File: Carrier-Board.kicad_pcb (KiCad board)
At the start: 2 copper layers, 92 x 96 mm, 42 parts, among them J1 CONN_3-6318491-6, J10 Conn_02x03_Odd_Even, J2 Conn_01x0, J3 Conn_02x26_Odd_Even, J4 SI-51009-F, J5 Conn_02x26_Odd_Even, J6 Conn_01x03_Male, J7 Conn_01x03_Male, J8 Conn_01x06_Male, J9 Conn_02x04_Odd_Even, SW1 SW_Push, SW2 SW_Push, SW3 SW_Push, U1 MPM3620, U2 MPM3620, U9 MSATA-Socket

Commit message: Change but3ton footprint
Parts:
- SW1, SW2, SW3: footprint Buttons_Switches_SMD:SW_SPST_PTS645 -> Buttons_Switches_SMD:SW_SPST_B3U-1000P
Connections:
- J1 pad 101: Net-(J1-Pad101) -> (no net)
- J1 pad 102: Net-(J1-Pad102) -> (no net)
- J1 pad 103: Net-(J1-Pad103) -> (no net)
- J1 pad 112: Net-(J1-Pad112) -> (no net)
- J1 pad 113: Net-(J1-Pad113) -> (no net)
- J1 pad 114: Net-(J1-Pad114) -> (no net)
- J1 pad 115: Net-(J1-Pad115) -> (no net)
- J1 pad 123: Net-(J1-Pad123) -> (no net)
- J1 pad 124: Net-(J1-Pad124) -> (no net)
- J1 pad 125: Net-(J1-Pad125) -> (no net)
- J1 pad 126: Net-(J1-Pad126) -> (no net)
- J1 pad 127: Net-(J1-Pad127) -> (no net)
- J1 pad 128: Net-(J1-Pad128) -> (no net)
- J1 pad 129: Net-(J1-Pad129) -> (no net)
- J1 pad 130: Net-(J1-Pad130) -> (no net)
- J1 pad 132: Net-(J1-Pad132) -> (no net)
- J1 pad 133: Net-(J1-Pad133) -> (no net)
- J1 pad 135: Net-(J1-Pad135) -> (no net)
- J1 pad 136: Net-(J1-Pad136) -> (no net)
- J1 pad 137: Net-(J1-Pad137) -> (no net)
- J1 pad 138: Net-(J1-Pad138) -> (no net)
- J1 pad 139: Net-(J1-Pad139) -> (no net)
- J1 pad 140: Net-(J1-Pad140) -> (no net)
- J1 pad 142: Net-(J1-Pad142) -> (no net)
- J1 pad 145: Net-(J1-Pad145) -> (no net)
- J1 pad 146: Net-(J1-Pad146) -> (no net)
- J1 pad 147: Net-(J1-Pad147) -> (no net)
- J1 pad 148: Net-(J1-Pad148) -> (no net)
- J1 pad 149: Net-(J1-Pad149) -> (no net)
- J1 pad 15: Net-(J1-Pad15) -> (no net)
- J1 pad 150: Net-(J1-Pad150) -> (no net)
- J1 pad 152: Net-(J1-Pad152) -> (no net)
- J1 pad 153: Net-(J1-Pad153) -> (no net)
- J1 pad 154: Net-(J1-Pad154) -> (no net)
- J1 pad 155: Net-(J1-Pad155) -> (no net)
- J1 pad 156: Net-(J1-Pad156) -> (no net)
- J1 pad 157: Net-(J1-Pad157) -> (no net)
- J1 pad 158: Net-(J1-Pad158) -> (no net)
- J1 pad 160: Net-(J1-Pad160) -> (no net)
- J1 pad 162: Net-(J1-Pad162) -> (no net)
- J1 pad 163: Net-(J1-Pad163) -> (no net)
- J1 pad 165: Net-(J1-Pad165) -> (no net)
- J1 pad 166: Net-(J1-Pad166) -> (no net)
- J1 pad 168: Net-(J1-Pad168) -> (no net)
- J1 pad 169: Net-(J1-Pad169) -> (no net)
- J1 pad 171: Net-(J1-Pad171) -> (no net)
- J1 pad 172: Net-(J1-Pad172) -> (no net)
- J1 pad 174: Net-(J1-Pad174) -> (no net)
- J1 pad 175: Net-(J1-Pad175) -> (no net)
- J1 pad 176: Net-(J1-Pad176) -> (no net)
- J1 pad 178: Net-(J1-Pad178) -> (no net)
- J1 pad 179: Net-(J1-Pad179) -> (no net)
- J1 pad 18: Net-(J1-Pad18) -> (no net)
- J1 pad 181: Net-(J1-Pad181) -> (no net)
- J1 pad 182: Net-(J1-Pad182) -> (no net)
- J1 pad 183: Net-(J1-Pad183) -> (no net)
- J1 pad 184: Net-(J1-Pad184) -> (no net)
- J1 pad 185: Net-(J1-Pad185) -> (no net)
- J1 pad 186: Net-(J1-Pad186) -> (no net)
- J1 pad 187: Net-(J1-Pad187) -> (no net)
- J1 pad 188: Net-(J1-Pad188) -> (no net)
- J1 pad 189: Net-(J1-Pad189) -> (no net)
- J1 pad 191: Net-(J1-Pad191) -> (no net)
- J1 pad 192: Net-(J1-Pad192) -> (no net)
- J1 pad 193: Net-(J1-Pad193) -> (no net)
- J1 pad 198: Net-(J1-Pad198) -> (no net)
- J1 pad 199: Net-(J1-Pad199) -> (no net)
- J1 pad 201: Net-(J1-Pad201) -> (no net)
- J1 pad 202: Net-(J1-Pad202) -> (no net)
- J1 pad 203: Net-(J1-Pad203) -> (no net)
- J1 pad 204: Net-(J1-Pad204) -> (no net)
- J1 pad 205: Net-(J1-Pad205) -> (no net)
- J1 pad 206: Net-(J1-Pad206) -> (no net)
- J1 pad 207: Net-(J1-Pad207) -> (no net)
- J1 pad 208: Net-(J1-Pad208) -> (no net)
- J1 pad 209: Net-(J1-Pad209) -> (no net)
- J1 pad 211: Net-(J1-Pad211) -> (no net)
- J1 pad 212: Net-(J1-Pad212) -> (no net)
- J1 pad 22: Net-(J1-Pad22) -> (no net)
- J1 pad 23: Net-(J1-Pad23) -> (no net)
- J1 pad 24: Net-(J1-Pad24) -> (no net)
- J1 pad 25: Net-(J1-Pad25) -> (no net)
- J1 pad 26: Net-(J1-Pad26) -> (no net)
- J1 pad 27: Net-(J1-Pad27) -> (no net)
- J1 pad 29: Net-(J1-Pad29) -> (no net)
- J1 pad 30: Net-(J1-Pad30) -> (no net)
- J1 pad 32: Net-(J1-Pad32) -> (no net)
- J1 pad 33: Net-(J1-Pad33) -> (no net)
- J1 pad 34: Net-(J1-Pad34) -> (no net)
- J1 pad 35: Net-(J1-Pad35) -> (no net)
- J1 pad 36: Net-(J1-Pad36) -> (no net)
- J1 pad 37: Net-(J1-Pad37) -> (no net)
- J1 pad 38: Net-(J1-Pad38) -> (no net)
- J1 pad 39: Net-(J1-Pad39) -> (no net)
- J1 pad 40: Net-(J1-Pad40) -> (no net)
- J1 pad 42: Net-(J1-Pad42) -> (no net)
- J1 pad 43: Net-(J1-Pad43) -> (no net)
- J1 pad 44: Net-(J1-Pad44) -> (no net)
- J1 pad 45: Net-(J1-Pad45) -> (no net)
- J1 pad 46: Net-(J1-Pad46) -> (no net)
- J1 pad 47: Net-(J1-Pad47) -> (no net)
- J1 pad 48: Net-(J1-Pad48) -> (no net)
- J1 pad 49: Net-(J1-Pad49) -> (no net)
- J1 pad 50: Net-(J1-Pad50) -> (no net)
- J1 pad 52: Net-(J1-Pad52) -> (no net)
- J1 pad 53: Net-(J1-Pad53) -> (no net)
- J1 pad 55: Net-(J1-Pad55) -> (no net)
- J1 pad 56: Net-(J1-Pad56) -> (no net)
- J1 pad 58: Net-(J1-Pad58) -> (no net)
- J1 pad 59: Net-(J1-Pad59) -> (no net)
- J1 pad 61: Net-(J1-Pad61) -> (no net)
- J1 pad 62: Net-(J1-Pad62) -> (no net)
- J1 pad 64: Net-(J1-Pad64) -> (no net)
- J1 pad 65: Net-(J1-Pad65) -> (no net)
- J1 pad 68: Net-(J1-Pad68) -> (no net)
- J1 pad 69: Net-(J1-Pad69) -> (no net)
- J1 pad 71: Net-(J1-Pad71) -> (no net)
- J1 pad 72: Net-(J1-Pad72) -> (no net)
- J1 pad 73: Net-(J1-Pad73) -> (no net)
- J1 pad 74: Net-(J1-Pad74) -> (no net)
- J1 pad 75: Net-(J1-Pad75) -> (no net)
- J1 pad 76: Net-(J1-Pad76) -> (no net)
- J1 pad 77: Net-(J1-Pad77) -> (no net)
- J1 pad 78: Net-(J1-Pad78) -> (no net)
- J1 pad 79: Net-(J1-Pad79) -> (no net)
- J1 pad 8: Net-(J1-Pad8) -> (no net)
- J1 pad 81: Net-(J1-Pad81) -> (no net)
- J1 pad 82: Net-(J1-Pad82) -> (no net)
- J1 pad 83: Net-(J1-Pad83) -> (no net)
- J1 pad 84: Net-(J1-Pad84) -> (no net)
- J1 pad 86: Net-(J1-Pad86) -> (no net)
- J1 pad 87: Net-(J1-Pad87) -> (no net)
- J1 pad 88: Net-(J1-Pad88) -> (no net)
- J1 pad 89: Net-(J1-Pad89) -> (no net)
- J1 pad 91: Net-(J1-Pad91) -> (no net)
- J1 pad 96: Net-(J1-Pad96) -> (no net)
- J10 pad 2: SPI_POWER -> (no net)
- J3 pad 1: Net-(J3-Pad1) -> (no net)
- J3 pad 10: Net-(J3-Pad10) -> (no net)
- J3 pad 11: Net-(J3-Pad11) -> (no net)
- J3 pad 12: Net-(J3-Pad12) -> (no net)
- J3 pad 13: Net-(J3-Pad13) -> (no net)
- J3 pad 14: Net-(J3-Pad14) -> (no net)
- J3 pad 15: Net-(J3-Pad15) -> (no net)
- J3 pad 16: Net-(J3-Pad16) -> (no net)
- J3 pad 17: Net-(J3-Pad17) -> (no net)
- J3 pad 18: Net-(J3-Pad18) -> (no net)
- J3 pad 19: Net-(J3-Pad19) -> (no net)
- J3 pad 2: Net-(J3-Pad2) -> (no net)
- J3 pad 20: Net-(J3-Pad20) -> (no net)
- J3 pad 21: Net-(J3-Pad21) -> (no net)
- J3 pad 22: Net-(J3-Pad22) -> (no net)
- J3 pad 23: Net-(J3-Pad23) -> (no net)
- J3 pad 24: Net-(J3-Pad24) -> (no net)
- J3 pad 25: Net-(J3-Pad25) -> (no net)
- J3 pad 26: Net-(J3-Pad26) -> (no net)
- J3 pad 27: Net-(J3-Pad27) -> (no net)
- J3 pad 28: Net-(J3-Pad28) -> (no net)
- J3 pad 29: Net-(J3-Pad29) -> (no net)
- J3 pad 3: Net-(J3-Pad3) -> (no net)
- J3 pad 30: Net-(J3-Pad30) -> (no net)
- J3 pad 31: Net-(J3-Pad31) -> (no net)
- J3 pad 32: Net-(J3-Pad32) -> (no net)
- J3 pad 33: Net-(J3-Pad33) -> (no net)
- J3 pad 34: Net-(J3-Pad34) -> (no net)
- J3 pad 35: Net-(J3-Pad35) -> (no net)
- J3 pad 36: Net-(J3-Pad36) -> (no net)
- J3 pad 37: Net-(J3-Pad37) -> (no net)
- J3 pad 38: Net-(J3-Pad38) -> (no net)
- J3 pad 39: Net-(J3-Pad39) -> (no net)
- J3 pad 4: Net-(J3-Pad4) -> (no net)
- J3 pad 40: Net-(J3-Pad40) -> (no net)
- J3 pad 41: Net-(J3-Pad41) -> (no net)
- J3 pad 42: Net-(J3-Pad42) -> (no net)
- J3 pad 43: Net-(J3-Pad43) -> (no net)
- J3 pad 44: Net-(J3-Pad44) -> (no net)
- J3 pad 45: Net-(J3-Pad45) -> (no net)
- J3 pad 46: Net-(J3-Pad46) -> (no net)
- J3 pad 47: Net-(J3-Pad47) -> (no net)
- J3 pad 48: Net-(J3-Pad48) -> (no net)
- J3 pad 49: Net-(J3-Pad49) -> (no net)
- J3 pad 5: Net-(J3-Pad5) -> (no net)
- J3 pad 50: Net-(J3-Pad50) -> (no net)
- J3 pad 51: Net-(J3-Pad51) -> (no net)
- J3 pad 52: Net-(J3-Pad52) -> (no net)
- J3 pad 6: Net-(J3-Pad6) -> (no net)
- J3 pad 7: Net-(J3-Pad7) -> (no net)
- J3 pad 8: Net-(J3-Pad8) -> (no net)
- J3 pad 9: Net-(J3-Pad9) -> (no net)
- J4 pad 14: Net-(J4-Pad14) -> (no net)
- J5 pad 1: Net-(J5-Pad1) -> (no net)
- J5 pad 10: Net-(J5-Pad10) -> (no net)
- J5 pad 11: Net-(J5-Pad11) -> (no net)
- J5 pad 12: Net-(J5-Pad12) -> (no net)
- J5 pad 13: Net-(J5-Pad13) -> (no net)
- J5 pad 14: Net-(J5-Pad14) -> (no net)
- J5 pad 15: Net-(J5-Pad15) -> (no net)
- J5 pad 16: Net-(J5-Pad16) -> (no net)
- J5 pad 17: Net-(J5-Pad17) -> (no net)
- J5 pad 18: Net-(J5-Pad18) -> (no net)
- J5 pad 19: Net-(J5-Pad19) -> (no net)
- J5 pad 2: Net-(J5-Pad2) -> (no net)
- J5 pad 20: Net-(J5-Pad20) -> (no net)
- J5 pad 21: Net-(J5-Pad21) -> (no net)
- J5 pad 22: Net-(J5-Pad22) -> (no net)
- J5 pad 23: Net-(J5-Pad23) -> (no net)
- J5 pad 24: Net-(J5-Pad24) -> (no net)
- J5 pad 25: Net-(J5-Pad25) -> (no net)
- J5 pad 26: Net-(J5-Pad26) -> (no net)
- J5 pad 27: Net-(J5-Pad27) -> (no net)
- J5 pad 28: Net-(J5-Pad28) -> (no net)
- J5 pad 29: Net-(J5-Pad29) -> (no net)
- J5 pad 3: Net-(J5-Pad3) -> (no net)
- J5 pad 30: Net-(J5-Pad30) -> (no net)
- J5 pad 31: Net-(J5-Pad31) -> (no net)
- J5 pad 32: Net-(J5-Pad32) -> (no net)
- J5 pad 33: Net-(J5-Pad33) -> (no net)
- J5 pad 34: Net-(J5-Pad34) -> (no net)
- J5 pad 35: Net-(J5-Pad35) -> (no net)
- J5 pad 36: Net-(J5-Pad36) -> (no net)
- J5 pad 37: Net-(J5-Pad37) -> (no net)
- J5 pad 38: Net-(J5-Pad38) -> (no net)
- J5 pad 39: Net-(J5-Pad39) -> (no net)
- J5 pad 4: Net-(J5-Pad4) -> (no net)
- J5 pad 40: Net-(J5-Pad40) -> (no net)
- J5 pad 41: Net-(J5-Pad41) -> (no net)
- J5 pad 42: Net-(J5-Pad42) -> (no net)
- J5 pad 43: Net-(J5-Pad43) -> (no net)
- J5 pad 44: Net-(J5-Pad44) -> (no net)
- J5 pad 45: Net-(J5-Pad45) -> (no net)
- J5 pad 46: Net-(J5-Pad46) -> (no net)
- J5 pad 47: Net-(J5-Pad47) -> (no net)
- J5 pad 48: Net-(J5-Pad48) -> (no net)
- J5 pad 49: Net-(J5-Pad49) -> (no net)
- J5 pad 5: Net-(J5-Pad5) -> (no net)
- J5 pad 50: Net-(J5-Pad50) -> (no net)
- J5 pad 51: Net-(J5-Pad51) -> (no net)
- J5 pad 52: Net-(J5-Pad52) -> (no net)
- J5 pad 6: Net-(J5-Pad6) -> (no net)
- J5 pad 7: Net-(J5-Pad7) -> (no net)
- J5 pad 8: Net-(J5-Pad8) -> (no net)
- J5 pad 9: Net-(J5-Pad9) -> (no net)
- J6 pad 1: Net-(J6-Pad1) -> (no net)
- U1 pad 11: Net-(U1-Pad11) -> (no net)
- U1 pad 2: Net-(U1-Pad2) -> (no net)
- U1 pad 4: Net-(U1-Pad4) -> (no net)
- U1 pad 5: Net-(U1-Pad5) -> (no net)
- U1 pad 6: Net-(U1-Pad6) -> (no net)
- U2 pad 11: Net-(U2-Pad11) -> (no net)
- U2 pad 2: Net-(U2-Pad2) -> (no net)
- U2 pad 4: Net-(U2-Pad4) -> (no net)
- U2 pad 5: Net-(U2-Pad5) -> (no net)
- U2 pad 6: Net-(U2-Pad6) -> (no net)
- U9 pad 1: Net-(U9-Pad1) -> (no net)
- U9 pad 10: Net-(U9-Pad10) -> (no net)
- U9 pad 11: Net-(U9-Pad11) -> (no net)
- U9 pad 12: Net-(U9-Pad12) -> (no net)
- U9 pad 13: Net-(U9-Pad13) -> (no net)
- U9 pad 14: Net-(U9-Pad14) -> (no net)
- U9 pad 16: Net-(U9-Pad16) -> (no net)
- U9 pad 17: Net-(U9-Pad17) -> (no net)
- U9 pad 19: Net-(U9-Pad19) -> (no net)
- U9 pad 20: Net-(U9-Pad20) -> (no net)
- U9 pad 22: Net-(U9-Pad22) -> (no net)
- U9 pad 28: Net-(U9-Pad28) -> (no net)
- U9 pad 3: Net-(U9-Pad3) -> (no net)
- U9 pad 30: Net-(U9-Pad30) -> (no net)
- U9 pad 32: Net-(U9-Pad32) -> (no net)
- U9 pad 36: Net-(U9-Pad36) -> (no net)
- U9 pad 38: Net-(U9-Pad38) -> (no net)
- U9 pad 42: Net-(U9-Pad42) -> (no net)
- U9 pad 43: Net-(U9-Pad43) -> (no net)
- U9 pad 44: Net-(U9-Pad44) -> (no net)
- U9 pad 45: Net-(U9-Pad45) -> (no net)
- U9 pad 46: Net-(U9-Pad46) -> (no net)
- U9 pad 47: Net-(U9-Pad47) -> (no net)
- U9 pad 48: Net-(U9-Pad48) -> (no net)
- U9 pad 5: Net-(U9-Pad5) -> (no net)
- U9 pad 6: Net-(U9-Pad6) -> (no net)
- U9 pad 7: Net-(U9-Pad7) -> (no net)
- U9 pad 8: Net-(U9-Pad8) -> (no net)

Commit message: started traces
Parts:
- added R10: 330, Resistors_SMD:R_0805, F.Cu at (155.5, 97.8)
- added R11: 10K, Resistors_SMD:R_0603, B.Cu at (87.6, 26.6)
- added R12: 10K, Resistors_SMD:R_0603, B.Cu at (89.4, 32.8)
- added R13: 10K, Resistors_SMD:R_0603, B.Cu at (89.4, 36.5)
- C1, C2, C3, C4: footprint BusSimulator:C22 -> Capacitors_SMD:C_0805; moved to F.Cu
- R1, R2, R3, R4, R5, R6, R7, R8, U1, U2: moved to F.Cu
- R32, R9: moved to B.Cu
- moved J6 89.4 mm to (169.7, 49.2), turned to 0 degrees
- moved J9 85.2 mm to (30.7, 35.5), turned to 0 degrees
- moved J10 83.3 mm to (61.4, 28.4), turned to 0 degrees
- moved R9 52.0 mm to (153.3, 96.1), turned to 270 degrees
- moved SW3 36.5 mm to (86.9, 36.4)
- moved SW2 29.9 mm to (86.9, 31.6)
- moved R25 28.7 mm to (130.0, 114.6), turned to 270 degrees
- moved D8 28.0 mm to (129.9, 113.9)
- moved R2 27.6 mm to (139.2, 108.8), turned to 180 degrees
- moved R1 25.9 mm to (142.4, 107.8), turned to 270 degrees
- moved C2 25.5 mm to (142.4, 104.0), turned to 90 degrees
- moved U1 25.3 mm to (137.9, 104.5)
- moved R4 22.6 mm to (133.9, 103.0), turned to 270 degrees
- moved D5 21.8 mm to (121.9, 111.2), turned to 270 degrees
- moved R3 21.7 mm to (136.9, 99.3), turned to 180 degrees
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- renumbered D7 to D6, D6 to D7
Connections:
- J1 pad 101: (no net) -> Net-(J1-Pad101)
- J1 pad 102: (no net) -> Net-(J1-Pad102)
- J1 pad 103: (no net) -> Net-(J1-Pad103)
- J1 pad 112: (no net) -> Net-(J1-Pad112)
- J1 pad 113: (no net) -> Net-(J1-Pad113)
- J1 pad 114: (no net) -> Net-(J1-Pad114)
- J1 pad 115: (no net) -> Net-(J1-Pad115)
- J1 pad 123: (no net) -> Net-(J1-Pad123)
- J1 pad 124: (no net) -> Net-(J1-Pad124)
- J1 pad 125: (no net) -> Net-(J1-Pad125)
- J1 pad 126: (no net) -> Net-(J1-Pad126)
- J1 pad 127: (no net) -> Net-(J1-Pad127)
- J1 pad 128: (no net) -> Net-(J1-Pad128)
- J1 pad 129: (no net) -> Net-(J1-Pad129)
- J1 pad 130: (no net) -> Net-(J1-Pad130)
- J1 pad 132: (no net) -> Net-(J1-Pad132)
- J1 pad 133: (no net) -> Net-(J1-Pad133)
- J1 pad 135: (no net) -> Net-(J1-Pad135)
- J1 pad 136: (no net) -> Net-(J1-Pad136)
- J1 pad 137: (no net) -> Net-(J1-Pad137)
- J1 pad 138: (no net) -> Net-(J1-Pad138)
- J1 pad 139: (no net) -> Net-(J1-Pad139)
- J1 pad 140: (no net) -> Net-(J1-Pad140)
- J1 pad 142: (no net) -> Net-(J1-Pad142)
- J1 pad 145: (no net) -> Net-(J1-Pad145)
- J1 pad 146: (no net) -> Net-(J1-Pad146)
- J1 pad 147: (no net) -> Net-(J1-Pad147)
- J1 pad 148: (no net) -> Net-(J1-Pad148)
- J1 pad 149: (no net) -> Net-(J1-Pad149)
- J1 pad 15: (no net) -> Net-(J1-Pad15)
- J1 pad 150: (no net) -> Net-(J1-Pad150)
- J1 pad 152: (no net) -> Net-(J1-Pad152)
- J1 pad 153: (no net) -> Net-(J1-Pad153)
- J1 pad 154: (no net) -> Net-(J1-Pad154)
- J1 pad 155: (no net) -> Net-(J1-Pad155)
- J1 pad 156: (no net) -> Net-(J1-Pad156)
- J1 pad 157: (no net) -> Net-(J1-Pad157)
- J1 pad 158: (no net) -> Net-(J1-Pad158)
- J1 pad 160: (no net) -> Net-(J1-Pad160)
- J1 pad 162: (no net) -> Net-(J1-Pad162)
- J1 pad 163: (no net) -> Net-(J1-Pad163)
- J1 pad 165: (no net) -> Net-(J1-Pad165)
- J1 pad 166: (no net) -> Net-(J1-Pad166)
- J1 pad 168: (no net) -> Net-(J1-Pad168)
- J1 pad 169: (no net) -> Net-(J1-Pad169)
- J1 pad 171: (no net) -> Net-(J1-Pad171)
- J1 pad 172: (no net) -> Net-(J1-Pad172)
- J1 pad 174: (no net) -> Net-(J1-Pad174)
- J1 pad 175: (no net) -> Net-(J1-Pad175)
- J1 pad 176: (no net) -> Net-(J1-Pad176)
- J1 pad 178: (no net) -> Net-(J1-Pad178)
- J1 pad 179: (no net) -> Net-(J1-Pad179)
- J1 pad 18: (no net) -> Net-(J1-Pad18)
- J1 pad 181: (no net) -> Net-(J1-Pad181)
- J1 pad 182: (no net) -> Net-(J1-Pad182)
- J1 pad 183: (no net) -> Net-(J1-Pad183)
- J1 pad 184: (no net) -> Net-(J1-Pad184)
- J1 pad 185: (no net) -> Net-(J1-Pad185)
- J1 pad 186: (no net) -> Net-(J1-Pad186)
- J1 pad 187: (no net) -> Net-(J1-Pad187)
- J1 pad 188: (no net) -> Net-(J1-Pad188)
- J1 pad 189: (no net) -> Net-(J1-Pad189)
- J1 pad 191: (no net) -> Net-(J1-Pad191)
- J1 pad 192: (no net) -> Net-(J1-Pad192)
- J1 pad 193: (no net) -> Net-(J1-Pad193)
- J1 pad 198: (no net) -> Net-(J1-Pad198)
- J1 pad 199: (no net) -> Net-(J1-Pad199)
- J1 pad 201: (no net) -> Net-(J1-Pad201)
- J1 pad 202: (no net) -> Net-(J1-Pad202)
- J1 pad 203: (no net) -> Net-(J1-Pad203)
- J1 pad 204: (no net) -> Net-(J1-Pad204)
- J1 pad 205: (no net) -> Net-(J1-Pad205)
- J1 pad 206: (no net) -> Net-(J1-Pad206)
- J1 pad 207: (no net) -> Net-(J1-Pad207)
- J1 pad 208: (no net) -> Net-(J1-Pad208)
- J1 pad 209: (no net) -> Net-(J1-Pad209)
- J1 pad 211: (no net) -> Net-(J1-Pad211)
- J1 pad 212: (no net) -> Net-(J1-Pad212)
- J1 pad 22: (no net) -> Net-(J1-Pad22)
- J1 pad 23: (no net) -> Net-(J1-Pad23)
- J1 pad 24: (no net) -> Net-(J1-Pad24)
- J1 pad 25: (no net) -> Net-(J1-Pad25)
- J1 pad 26: (no net) -> Net-(J1-Pad26)
- J1 pad 27: (no net) -> Net-(J1-Pad27)
- J1 pad 29: (no net) -> Net-(J1-Pad29)
- J1 pad 30: (no net) -> Net-(J1-Pad30)
- J1 pad 32: (no net) -> Net-(J1-Pad32)
- J1 pad 33: (no net) -> Net-(J1-Pad33)
- J1 pad 34: (no net) -> Net-(J1-Pad34)
- J1 pad 35: (no net) -> Net-(J1-Pad35)
- J1 pad 36: (no net) -> Net-(J1-Pad36)
- J1 pad 37: (no net) -> Net-(J1-Pad37)
- J1 pad 38: (no net) -> Net-(J1-Pad38)
- J1 pad 39: (no net) -> Net-(J1-Pad39)
- J1 pad 40: (no net) -> Net-(J1-Pad40)
- J1 pad 42: (no net) -> Net-(J1-Pad42)
- J1 pad 43: (no net) -> Net-(J1-Pad43)
- J1 pad 44: (no net) -> Net-(J1-Pad44)
- J1 pad 45: (no net) -> Net-(J1-Pad45)
- J1 pad 46: (no net) -> Net-(J1-Pad46)
- J1 pad 47: (no net) -> Net-(J1-Pad47)
- J1 pad 48: (no net) -> Net-(J1-Pad48)
- J1 pad 49: (no net) -> Net-(J1-Pad49)
- J1 pad 50: (no net) -> Net-(J1-Pad50)
- J1 pad 52: (no net) -> Net-(J1-Pad52)
- J1 pad 53: (no net) -> Net-(J1-Pad53)
- J1 pad 55: (no net) -> Net-(J1-Pad55)
- J1 pad 56: (no net) -> Net-(J1-Pad56)
- J1 pad 58: (no net) -> Net-(J1-Pad58)
- J1 pad 59: (no net) -> Net-(J1-Pad59)
- J1 pad 61: (no net) -> Net-(J1-Pad61)
- J1 pad 62: (no net) -> Net-(J1-Pad62)
- J1 pad 64: (no net) -> Net-(J1-Pad64)
- J1 pad 65: (no net) -> Net-(J1-Pad65)
- J1 pad 68: (no net) -> Net-(J1-Pad68)
- J1 pad 69: (no net) -> Net-(J1-Pad69)
- J1 pad 71: (no net) -> Net-(J1-Pad71)
- J1 pad 72: (no net) -> Net-(J1-Pad72)
- J1 pad 73: (no net) -> Net-(J1-Pad73)
- J1 pad 74: (no net) -> Net-(J1-Pad74)
- J1 pad 75: (no net) -> Net-(J1-Pad75)
- J1 pad 76: (no net) -> Net-(J1-Pad76)
- J1 pad 77: (no net) -> Net-(J1-Pad77)
- J1 pad 78: (no net) -> Net-(J1-Pad78)
- J1 pad 79: (no net) -> Net-(J1-Pad79)
- J1 pad 8: (no net) -> Net-(J1-Pad8)
- J1 pad 81: (no net) -> Net-(J1-Pad81)
- J1 pad 82: (no net) -> Net-(J1-Pad82)
- J1 pad 83: (no net) -> Net-(J1-Pad83)
- J1 pad 84: (no net) -> Net-(J1-Pad84)
- J1 pad 86: (no net) -> Net-(J1-Pad86)
- J1 pad 87: (no net) -> Net-(J1-Pad87)
- J1 pad 88: (no net) -> Net-(J1-Pad88)
- J1 pad 89: (no net) -> Net-(J1-Pad89)
- J1 pad 91: (no net) -> Net-(J1-Pad91)
- J1 pad 96: (no net) -> Net-(J1-Pad96)
- J1 pad TAB1: (no net) -> GBE0_CTREF(GND)
- J10 pad 2: (no net) -> SPI_POWER
- J3 pad 1: (no net) -> Net-(J3-Pad1)
- J3 pad 10: (no net) -> Net-(J3-Pad10)
- J3 pad 11: (no net) -> Net-(J3-Pad11)
- J3 pad 12: (no net) -> Net-(J3-Pad12)
- J3 pad 13: (no net) -> Net-(J3-Pad13)
- J3 pad 14: (no net) -> Net-(J3-Pad14)
- J3 pad 15: (no net) -> Net-(J3-Pad15)
- J3 pad 16: (no net) -> Net-(J3-Pad16)
- J3 pad 17: (no net) -> Net-(J3-Pad17)
- J3 pad 18: (no net) -> Net-(J3-Pad18)
- J3 pad 19: (no net) -> Net-(J3-Pad19)
- J3 pad 2: (no net) -> Net-(J3-Pad2)
- J3 pad 20: (no net) -> Net-(J3-Pad20)
- J3 pad 21: (no net) -> Net-(J3-Pad21)
- J3 pad 22: (no net) -> Net-(J3-Pad22)
- J3 pad 23: (no net) -> Net-(J3-Pad23)
- J3 pad 24: (no net) -> Net-(J3-Pad24)
- J3 pad 25: (no net) -> Net-(J3-Pad25)
- J3 pad 26: (no net) -> Net-(J3-Pad26)
- J3 pad 27: (no net) -> Net-(J3-Pad27)
- J3 pad 28: (no net) -> Net-(J3-Pad28)
- J3 pad 29: (no net) -> Net-(J3-Pad29)
- J3 pad 3: (no net) -> Net-(J3-Pad3)
- J3 pad 30: (no net) -> Net-(J3-Pad30)
- J3 pad 31: (no net) -> Net-(J3-Pad31)
- J3 pad 32: (no net) -> Net-(J3-Pad32)
- J3 pad 33: (no net) -> Net-(J3-Pad33)
- J3 pad 34: (no net) -> Net-(J3-Pad34)
- J3 pad 35: (no net) -> Net-(J3-Pad35)
- J3 pad 36: (no net) -> Net-(J3-Pad36)
- J3 pad 37: (no net) -> Net-(J3-Pad37)
- J3 pad 38: (no net) -> Net-(J3-Pad38)
- J3 pad 39: (no net) -> Net-(J3-Pad39)
- J3 pad 4: (no net) -> Net-(J3-Pad4)
- J3 pad 40: (no net) -> Net-(J3-Pad40)
- J3 pad 41: (no net) -> Net-(J3-Pad41)
- J3 pad 42: (no net) -> Net-(J3-Pad42)
- J3 pad 43: (no net) -> Net-(J3-Pad43)
- J3 pad 44: (no net) -> Net-(J3-Pad44)
- J3 pad 45: (no net) -> Net-(J3-Pad45)
- J3 pad 46: (no net) -> Net-(J3-Pad46)
- J3 pad 47: (no net) -> Net-(J3-Pad47)
- J3 pad 48: (no net) -> Net-(J3-Pad48)
- J3 pad 49: (no net) -> Net-(J3-Pad49)
- J3 pad 5: (no net) -> Net-(J3-Pad5)
- J3 pad 50: (no net) -> Net-(J3-Pad50)
- J3 pad 51: (no net) -> Net-(J3-Pad51)
- J3 pad 52: (no net) -> Net-(J3-Pad52)
- J3 pad 6: (no net) -> Net-(J3-Pad6)
- J3 pad 7: (no net) -> Net-(J3-Pad7)
- J3 pad 8: (no net) -> Net-(J3-Pad8)
- J3 pad 9: (no net) -> Net-(J3-Pad9)
- J4 pad 14: (no net) -> Net-(J4-Pad14)
- J5 pad 1: (no net) -> Net-(J5-Pad1)
- J5 pad 10: (no net) -> Net-(J5-Pad10)
- J5 pad 11: (no net) -> Net-(J5-Pad11)
- J5 pad 12: (no net) -> Net-(J5-Pad12)
- J5 pad 13: (no net) -> Net-(J5-Pad13)
- J5 pad 14: (no net) -> Net-(J5-Pad14)
- J5 pad 15: (no net) -> Net-(J5-Pad15)
- J5 pad 16: (no net) -> Net-(J5-Pad16)
- J5 pad 17: (no net) -> Net-(J5-Pad17)
- J5 pad 18: (no net) -> Net-(J5-Pad18)
- J5 pad 19: (no net) -> Net-(J5-Pad19)
- J5 pad 2: (no net) -> Net-(J5-Pad2)
- J5 pad 20: (no net) -> Net-(J5-Pad20)
- J5 pad 21: (no net) -> Net-(J5-Pad21)
- J5 pad 22: (no net) -> Net-(J5-Pad22)
- J5 pad 23: (no net) -> Net-(J5-Pad23)
- J5 pad 24: (no net) -> Net-(J5-Pad24)
- J5 pad 25: (no net) -> Net-(J5-Pad25)
- J5 pad 26: (no net) -> Net-(J5-Pad26)
- J5 pad 27: (no net) -> Net-(J5-Pad27)
- J5 pad 28: (no net) -> Net-(J5-Pad28)
- J5 pad 29: (no net) -> Net-(J5-Pad29)
- J5 pad 3: (no net) -> Net-(J5-Pad3)
- J5 pad 30: (no net) -> Net-(J5-Pad30)
- J5 pad 31: (no net) -> Net-(J5-Pad31)
- J5 pad 32: (no net) -> Net-(J5-Pad32)
- J5 pad 33: (no net) -> Net-(J5-Pad33)
- J5 pad 34: (no net) -> Net-(J5-Pad34)
- J5 pad 35: (no net) -> Net-(J5-Pad35)
- J5 pad 36: (no net) -> Net-(J5-Pad36)
- J5 pad 37: (no net) -> Net-(J5-Pad37)
- J5 pad 38: (no net) -> Net-(J5-Pad38)
- J5 pad 39: (no net) -> Net-(J5-Pad39)
- J5 pad 4: (no net) -> Net-(J5-Pad4)
- J5 pad 40: (no net) -> Net-(J5-Pad40)
- J5 pad 41: (no net) -> Net-(J5-Pad41)
- J5 pad 42: (no net) -> Net-(J5-Pad42)
- J5 pad 43: (no net) -> Net-(J5-Pad43)
- J5 pad 44: (no net) -> Net-(J5-Pad44)
- J5 pad 45: (no net) -> Net-(J5-Pad45)
- J5 pad 46: (no net) -> Net-(J5-Pad46)
- J5 pad 47: (no net) -> Net-(J5-Pad47)
- J5 pad 48: (no net) -> Net-(J5-Pad48)
- J5 pad 49: (no net) -> Net-(J5-Pad49)
- J5 pad 5: (no net) -> Net-(J5-Pad5)
- J5 pad 50: (no net) -> Net-(J5-Pad50)
- J5 pad 51: (no net) -> Net-(J5-Pad51)
- J5 pad 52: (no net) -> Net-(J5-Pad52)
- J5 pad 6: (no net) -> Net-(J5-Pad6)
- J5 pad 7: (no net) -> Net-(J5-Pad7)
- J5 pad 8: (no net) -> Net-(J5-Pad8)
- J5 pad 9: (no net) -> Net-(J5-Pad9)
- J6 pad 1: (no net) -> GBE0_CTREF(GND)
- U1 pad 11: (no net) -> Net-(U1-Pad11)
- U1 pad 2: (no net) -> Net-(U1-Pad2)
- U1 pad 4: (no net) -> Net-(U1-Pad4)
- U1 pad 5: (no net) -> Net-(U1-Pad5)
- U1 pad 6: (no net) -> Net-(U1-Pad6)
- U2 pad 11: (no net) -> Net-(U2-Pad11)
- U2 pad 2: (no net) -> Net-(U2-Pad2)
- U2 pad 4: (no net) -> Net-(U2-Pad4)
- U2 pad 5: (no net) -> Net-(U2-Pad5)
- U2 pad 6: (no net) -> Net-(U2-Pad6)
- U9 pad 1: (no net) -> Net-(U9-Pad1)
- U9 pad 10: (no net) -> Net-(U9-Pad10)
- U9 pad 11: (no net) -> Net-(U9-Pad11)
- U9 pad 12: (no net) -> Net-(U9-Pad12)
- U9 pad 13: (no net) -> Net-(U9-Pad13)
- U9 pad 14: (no net) -> Net-(U9-Pad14)
- U9 pad 16: (no net) -> Net-(U9-Pad16)
- U9 pad 17: (no net) -> Net-(U9-Pad17)
- U9 pad 19: (no net) -> Net-(U9-Pad19)
- U9 pad 20: (no net) -> Net-(U9-Pad20)
- U9 pad 22: (no net) -> Net-(U9-Pad22)
- U9 pad 28: (no net) -> Net-(U9-Pad28)
- U9 pad 3: (no net) -> Net-(U9-Pad3)
- U9 pad 30: (no net) -> Net-(U9-Pad30)
- U9 pad 32: (no net) -> Net-(U9-Pad32)
- U9 pad 36: (no net) -> Net-(U9-Pad36)
- U9 pad 38: (no net) -> Net-(U9-Pad38)
- U9 pad 42: (no net) -> Net-(U9-Pad42)
- U9 pad 43: (no net) -> Net-(U9-Pad43)
- U9 pad 44: (no net) -> Net-(U9-Pad44)
- U9 pad 45: (no net) -> Net-(U9-Pad45)
- U9 pad 46: (no net) -> Net-(U9-Pad46)
- U9 pad 47: (no net) -> Net-(U9-Pad47)
- U9 pad 48: (no net) -> Net-(U9-Pad48)
- U9 pad 5: (no net) -> Net-(U9-Pad5)
- U9 pad 6: (no net) -> Net-(U9-Pad6)
- U9 pad 7: (no net) -> Net-(U9-Pad7)
- U9 pad 8: (no net) -> Net-(U9-Pad8)
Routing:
- net GBE0_CTREF(GND): track 0.00 -> 168.0 mm, vias 0 -> 2
- net mCOM_12V: track 0.00 -> 120.9 mm, vias 0 -> 1
- net PWR_OK: track 0.00 -> 64.4 mm, vias 0 -> 1
- net GBE0_LINK1000#: track 0.00 -> 64.2 mm, vias 0 -> 2
- net GBE0_LINK100#: track 0.00 -> 59.4 mm
- net mCOM_RX: track 0.00 -> 47.3 mm
- net mCOM_TX: track 0.00 -> 42.8 mm, vias 0 -> 2
- net +3.3V: track 0.00 -> 41.2 mm
- net mCOM_5V_SBY: track 0.00 -> 39.1 mm, vias 0 -> 2
- net I2C_DAT: track 0.00 -> 33.5 mm, vias 0 -> 2
- net I2C_CK: track 0.00 -> 32.7 mm, vias 0 -> 2
- net PWRBTNn: track 0.00 -> 31.2 mm, vias 0 -> 2
- net SYS_RESETn: track 0.00 -> 29.9 mm, vias 0 -> 2
- net WAKE1n: track 0.00 -> 26.8 mm, vias 0 -> 1
- net SLEEPn: track 0.00 -> 25.2 mm, vias 0 -> 1
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- added copper zone on F.Cu, net +3.3V
- added copper zone on F.Cu, net mCOM_12V
- added copper zone on F.Cu, net mCOM_5V_SBY
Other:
- net class Default: clearance 0.2 -> 0.1; trace_width 0.25 -> 0.2
- rule trace_clearance: 0.2 -> 0.1

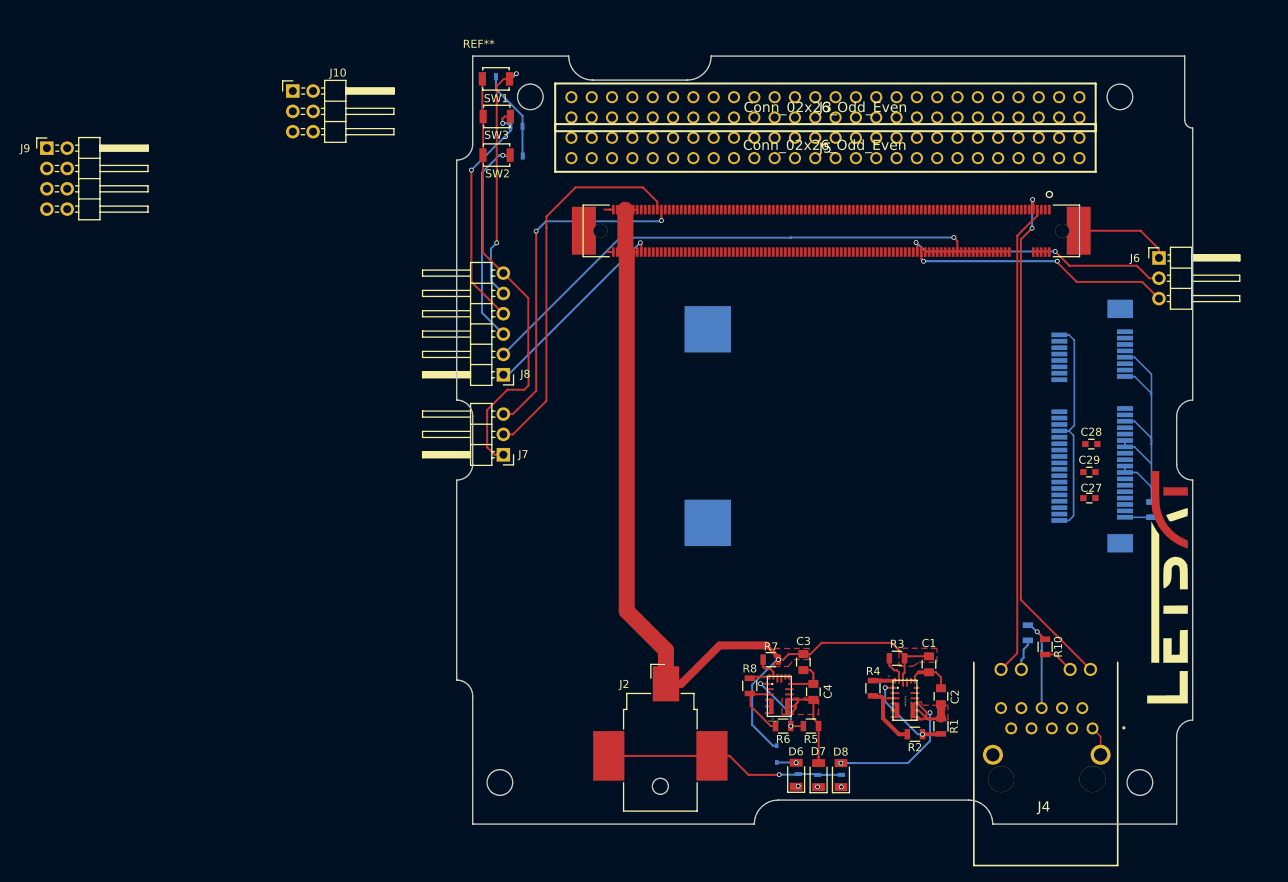
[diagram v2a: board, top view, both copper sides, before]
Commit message: added more traces
Sata finished

i2c ansd misc shit done

need:
gpio
spi
ethernet
ground planes
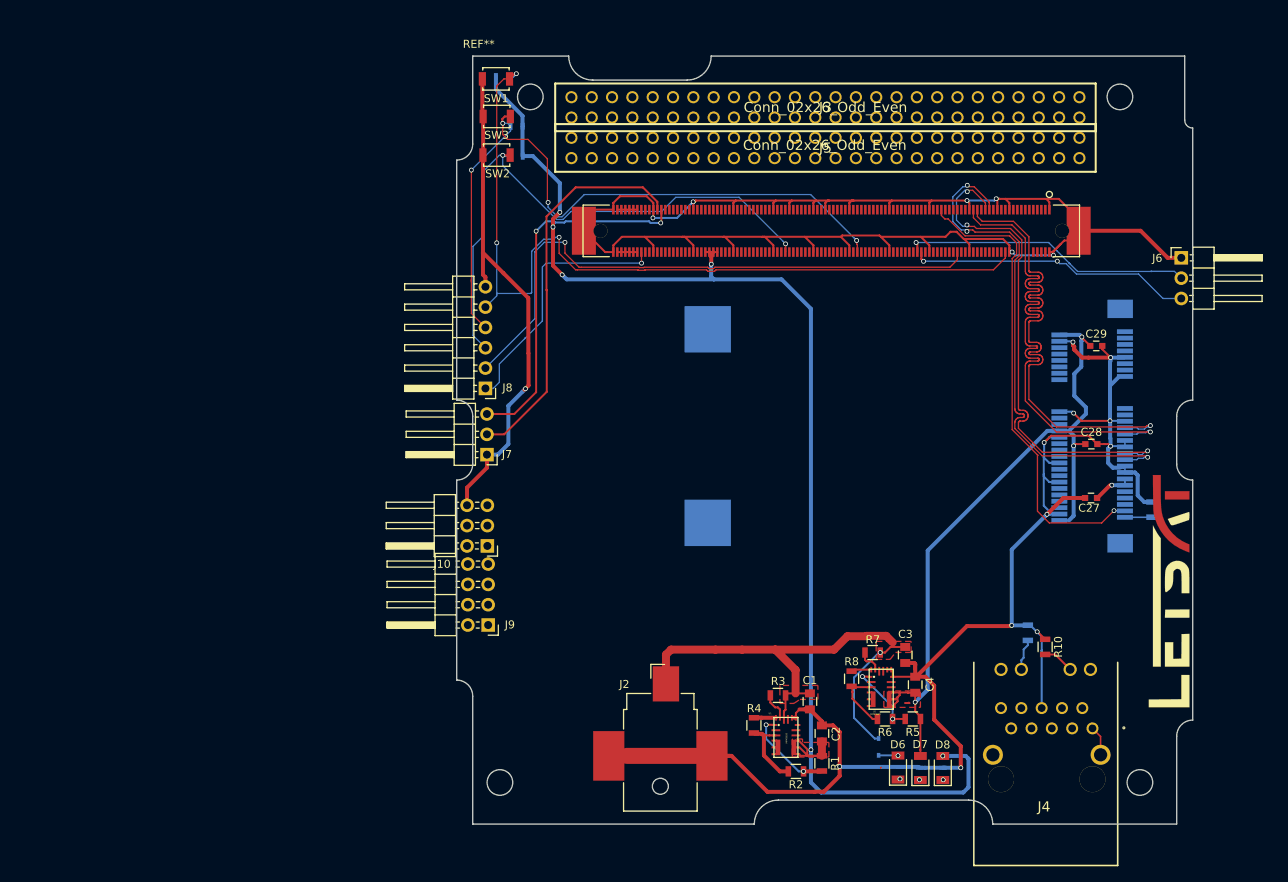
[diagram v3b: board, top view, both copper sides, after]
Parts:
- moved J9 81.2 mm to (85.8, 95.1), turned to 180 degrees
- moved J10 61.8 mm to (85.8, 85.2), turned to 180 degrees
- moved C29 15.8 mm to (161.9, 60.2)
- moved C1 15.6 mm to (126.1, 104.7)
- moved C2 15.6 mm to (127.6, 108.7)
- moved R1 15.6 mm to (127.6, 112.4)
- moved R2 15.6 mm to (124.3, 113.4)
- moved R3 15.6 mm to (122.1, 103.9)
- moved R4 15.6 mm to (119.1, 107.7)
- moved U1 15.6 mm to (123.1, 109.2)
- moved D6 12.8 mm to (137.1, 112.9)
- moved D8 12.8 mm to (142.7, 113.0)
- moved R24 12.8 mm to (137.3, 113.6)
- moved R6 12.8 mm to (135.5, 106.9)
- moved D5 12.8 mm to (134.7, 110.4)
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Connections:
- J1 pad TAB2: (no net) -> GBE0_CTREF(GND)
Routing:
- net GBE0_CTREF(GND): track 168.0 -> 477.5 mm, vias 2 -> 18
- net mCOM_5V_SBY: track 39.1 -> 164.7 mm, vias 2 -> 6
- net PWRBTNn: track 31.2 -> 106.4 mm, vias 2 -> 3
- net SATA0_RX-: track 0.00 -> 66.0 mm, vias 0 -> 1
- net SATA0_TX+: track 0.00 -> 66.0 mm, vias 0 -> 3
- net SATA0_RX+: track 0.00 -> 65.2 mm, vias 0 -> 1
- net GBE0_LINK1000#: track 64.2 -> 0.00 mm, vias 2 -> 0
- net SATA0_TX-: track 0.00 -> 63.7 mm, vias 0 -> 3
- net SYS_RESETn: track 29.9 -> 89.8 mm, vias 2 -> 4
- net GBE0_LINK100#: track 59.4 -> 0.00 mm
- net SATA_ACTn: track 0.00 -> 58.9 mm, vias 0 -> 1
- net +3.3V: track 41.2 -> 94.3 mm, vias 0 -> 4
- net mCOM_12V: track 120.9 -> 68.8 mm
- net WAKE1n: track 26.8 -> 72.5 mm, vias 1 -> 2
- net PWR_OK: track 64.4 -> 74.0 mm
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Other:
- net class Default: clearance 0.1 -> 0.2; trace_width 0.2 -> 0.25
- net class Power added: clearance 0.2, trace_width 0.5, via_dia 0.6, via_drill 0.4
- net class Signal added: clearance 0.2, trace_width 0.127, via_dia 0.6, via_drill 0.4
- rule trace_clearance: 0.1 -> 0.2
- rule trace_min: 0.2 -> 0.127

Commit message: 4 layer switch
changed to 4 layer
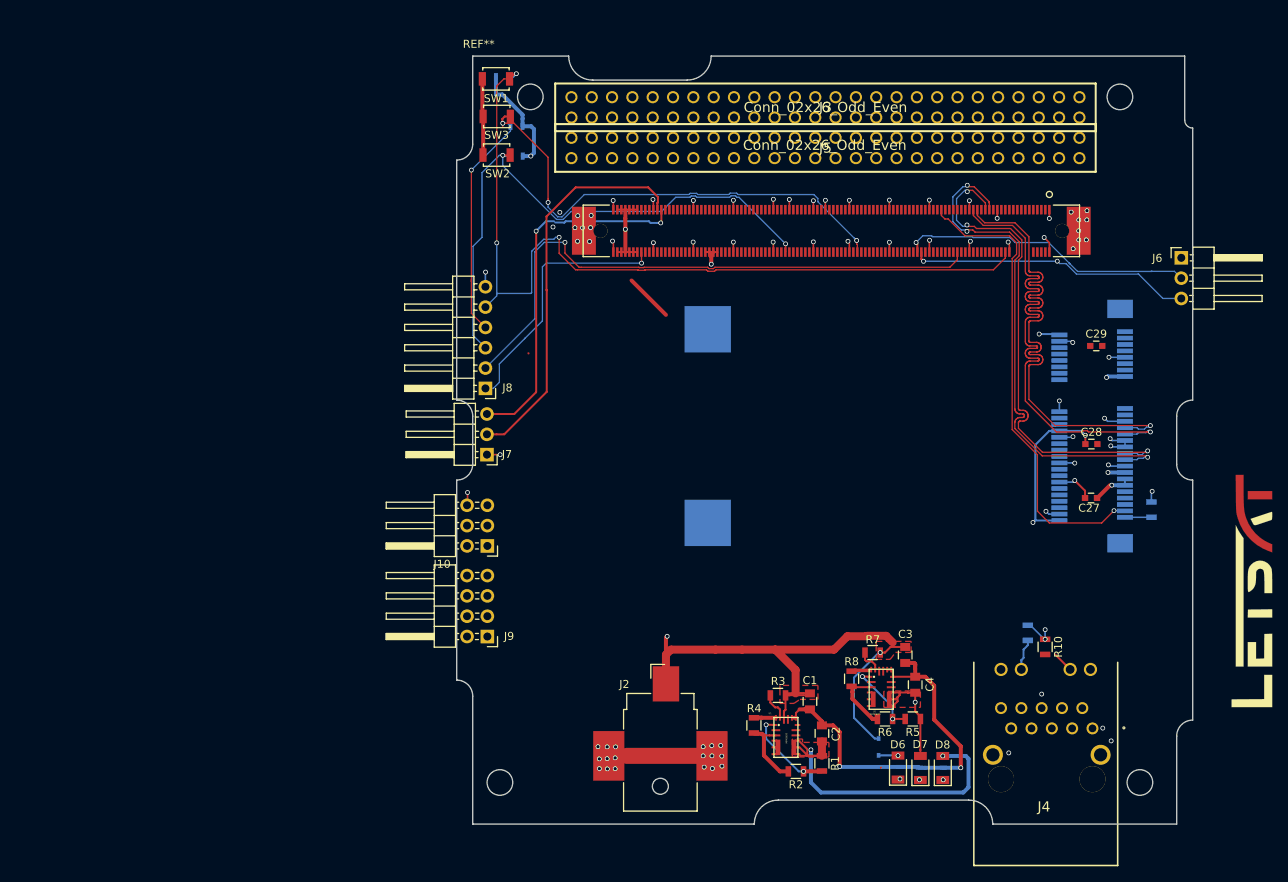
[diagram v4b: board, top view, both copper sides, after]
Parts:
- moved G1 10.4 mm to (181.6, 90.7)
- moved J9 1.44 mm to (85.8, 96.6)
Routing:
- net GBE0_CTREF(GND): track 477.5 -> 166.3 mm, vias 18 -> 84
- net mCOM_12V: track 68.8 -> 147.6 mm, vias 1 -> 3
- net +3.3V: track 94.3 -> 119.0 mm, vias 4 -> 5
- net mCOM_5V_SBY: track 164.7 -> 159.4 mm
- net Net-(R8-Pad1): track 2.47 -> 5.00 mm
- net (no net): track 1.68 -> 0.04 mm
- net Net-(J4-Pad14): track 3.90 -> 2.64 mm
- net I2C_DAT: track 36.7 -> 37.4 mm
- added copper zone on In1.Cu, net GBE0_CTREF(GND)
- added copper zone on In2.Cu, net GBE0_CTREF(GND)
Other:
- copper layers 2 -> 4
- net class ETHERNET added: clearance 0.1, trace_width 0.127, via_dia 0.6, via_drill 0.4
- rule trace_min: 0.127 -> 0.1

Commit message: ethernet
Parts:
- R9: moved to F.Cu
- moved R10 5.39 mm to (160.8, 97.1)
- moved R9 2.06 mm to (151.3, 96.7)
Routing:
- net GBE0_MDI3+: track 0.00 -> 107.7 mm, vias 0 -> 2
- net GBE0_MDI3-: track 0.00 -> 107.4 mm, vias 0 -> 2
- net GBE0_MDI1-: track 0.00 -> 75.8 mm, vias 0 -> 2
- net GBE0_MDI1+: track 0.00 -> 74.9 mm, vias 0 -> 2
- net GBE0_MDI0-: track 0.00 -> 28.7 mm
- net GBE0_MDI2+: track 0.00 -> 27.9 mm
- net GBE0_MDI0+: track 0.00 -> 26.5 mm
- net GBE0_MDI2-: track 0.00 -> 26.2 mm
- net GBE0_LINK1000#: track 0.00 -> 21.2 mm
- net GBE0_LINK100#: track 0.00 -> 17.3 mm
- net mCOM_12V: track 147.6 -> 141.5 mm
- net GBE0_CTREF(GND): track 166.3 -> 163.5 mm
- net Net-(J4-Pad14): track 2.64 -> 4.42 mm
- net (no net): track 0.04 -> 1.64 mm, vias 0 -> 2
- net mCOM_5V_SBY: vias 6 -> 4
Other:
- net class Power: trace_width 0.5 -> 0.2
